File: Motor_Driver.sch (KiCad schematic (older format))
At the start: 43 parts, among them CN3 CONN_HEADER_R_A_2POS_2.5MM, Q14 AOD4185, Q5 2N7002BK, Q6 2N7002BK, Q7 2N7002BK, U7 LMC6772AIMX-1, U8 VNH5019ATR-E, U9 LMC6772AIMX_2

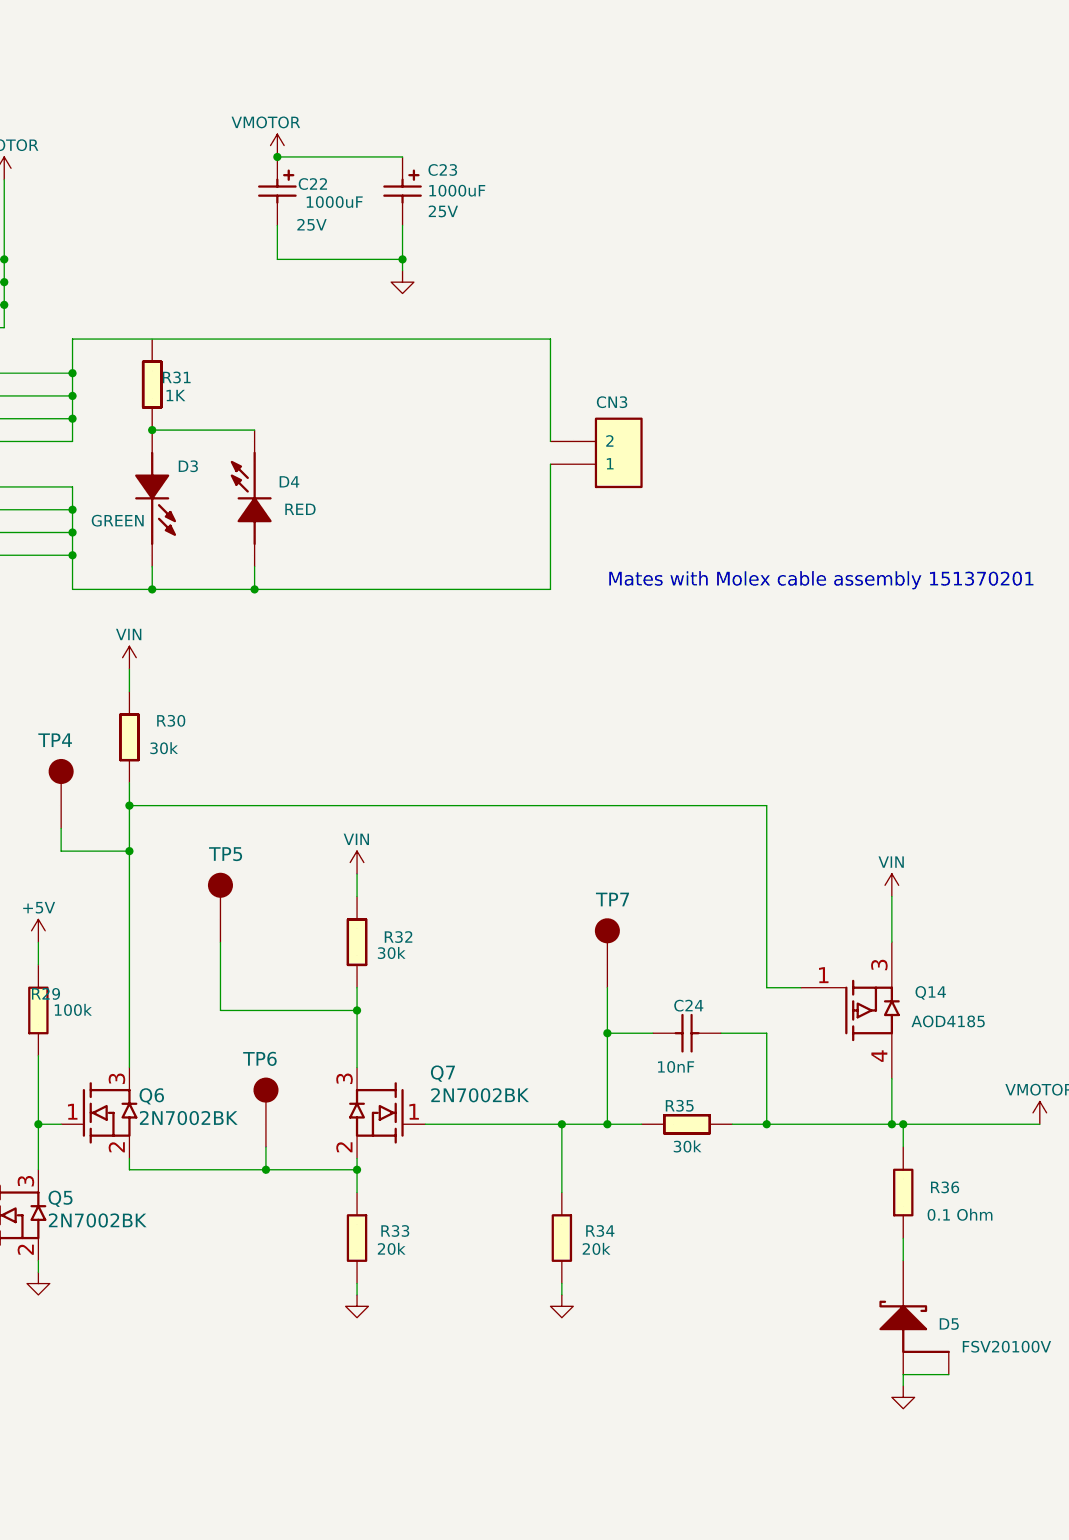
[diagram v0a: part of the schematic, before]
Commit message: Still had some text cleanups to do plus fixed a couple of minor circuit issues.
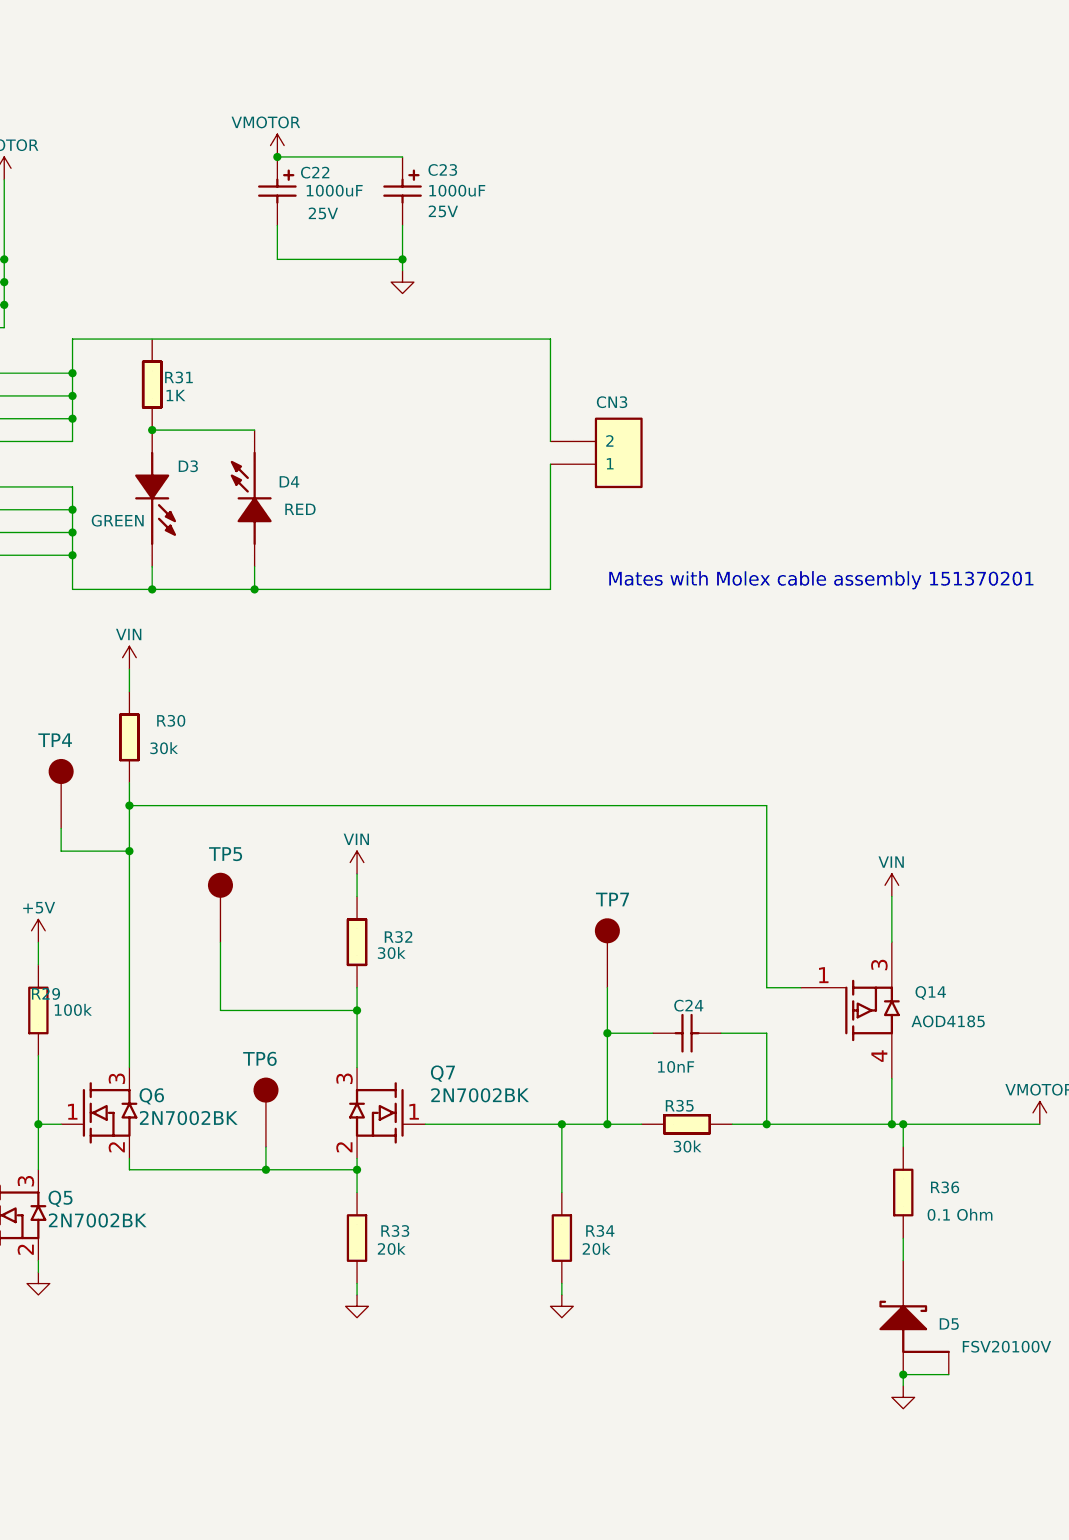
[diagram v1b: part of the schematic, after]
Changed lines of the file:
@@
 U 1 1 5F8DD0F1
 P 7050 1600
-F 0 "R31" V 7150 1540 50  0000 L BNN
+F 0 "R31" V 7150 1550 50  0000 L BNN
 F 1 "1K_0603_Chip_Resistor,_1%,_0.1W" V 7250 1550 50  0001 C CNN
 F 2 "" H 7350 1540 60  0001 C CNN
@@
 U 1 1 5F8DD0EF
 P 7500 700
-F 0 "C22" V 7650 790 50  0000 L BNN
+F 0 "C22" V 7600 800 50  0000 L BNN
 F 1 "1000uF_25V_Aluminium_SMD_Capacitor,_20%" V 7750 790 50  0001 C CNN
 F 2 "" H 7500 700 60  0001 C CNN
 F 3 "" H 7500 700 60  0001 C CNN
-F 4 "1000uF" V 7700 950 50  0000 C CNN "Val"
-F 5 "25V" V 7800 850 50  0000 C CNN "Voltage"
+F 4 "1000uF" V 7650 950 50  0000 C CNN "Val"
+F 5 "25V" V 7750 900 50  0000 C CNN "Voltage"
 	1    7500 700
 	0    1    1    0
@@
 Wire Wire Line
 	6950 1900 7400 1900
+Connection ~ 10250 6050
 $EndSCHEMATC

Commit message: Updating my local branch, wip Friday 10/30/20.  Got sucked into fixing up the libraries for the BOM...
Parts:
- removed U7: LMC6772AIMX-1, symbol OpenVent:LMC6772AIMX-1
- removed U9: LMC6772AIMX_2, symbol OpenVent:LMC6772AIMX_2
- added U7: LMC6772AIMX, Package_SO:SO-8_3.9x4.9mm_P1.27mm, symbol OpenVent:LMC6772AIMX
- C21: footprint (none) -> Capacitor_SMD:C_0603_1608Metric
- C24: footprint (none) -> Capacitor_SMD:C_0603_1608Metric; Voltage Rating 50V -> (none)
- CN3: Manufacturer Molex -> (none); ManufacturerPN 0534260210 -> (none); Mfr (none) -> Molex; Mfr_PN (none) -> 0534260210
- D3: footprint (none) -> LED_SMD:LED_0603_1608Metric; Spice Prefix D -> (none)
- D4: footprint (none) -> LED_SMD:LED_0603_1608Metric
- D5: footprint (none) -> Package_TO_SOT_SMD:TO-277A; Current (none) -> 20A; Desc (none) -> DIODE SCHOTTKY 100V 20A TO277-3; Detailed (none) -> Diode Schottky 20A Surface Mount TO-277-3; DistName (none) -> DigiKey; Dist_PN (none) -> FSV20100VTR-ND; Mfr (none) -> ON Semiconductor; Mfr_PN (none) -> FSV20100V; Voltage (none) -> 100V
- Q14: footprint (none) -> Package_TO_SOT_SMD:TO-252-2; Current (none) -> 40A; Desc (none) -> MOSFET P-CH 40V 40A TO252; DistName (none) -> DigiKey; Dist_PN (none) -> 785-1222-2-ND; Mfr (none) -> Alpha & Omega Semiconductor Inc.; Voltage (none) -> 40V
- Q5, Q6, Q7: footprint (none) -> Package_TO_SOT_SMD:SOT-23
- R16, R17, R18, R19, R20, R21, R22, R23, R24, R25, R27, R28, R29, R30, R31, R32, R33, R34, R35, R36: footprint (none) -> Resistor_SMD:R_0603_1608Metric
- R26: Manufacturer Vishay Dale -> (none); Mfr (none) -> Vishay Dale
- TP1, TP2, TP3, TP4, TP5, TP6, TP7: value ~ -> Test_Point_PTH; footprint (none) -> TestPoint:TestPoint_Pad_2.0x2.0mm
- U8: footprint (none) -> Package_SO:ST_MultiPowerSO-30; Desc (none) -> IC MTR DRV 5.5-24V MULTIPWRSO-30; Detailed (none) -> - Motor Driver Power MOSFET Parallel, PWM MultiPowerSO-30; DistName (none) -> DigiKey; Dist_PN (none) -> 497-13073-2-ND; Manufacturer ST Microelectronics -> (none); ManufacturerPN VNH5019ATR-E -> (none); Mfr (none) -> STMicroelectronics; Mfr_PN (none) -> VNH5019ATR-E

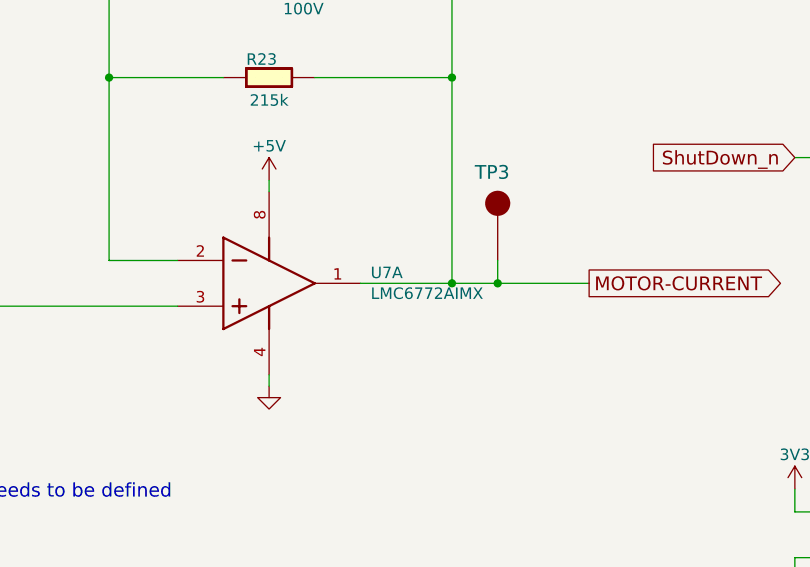
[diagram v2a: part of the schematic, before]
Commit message: Continuing on with library updates.  Started to fix up the USB interfaces.
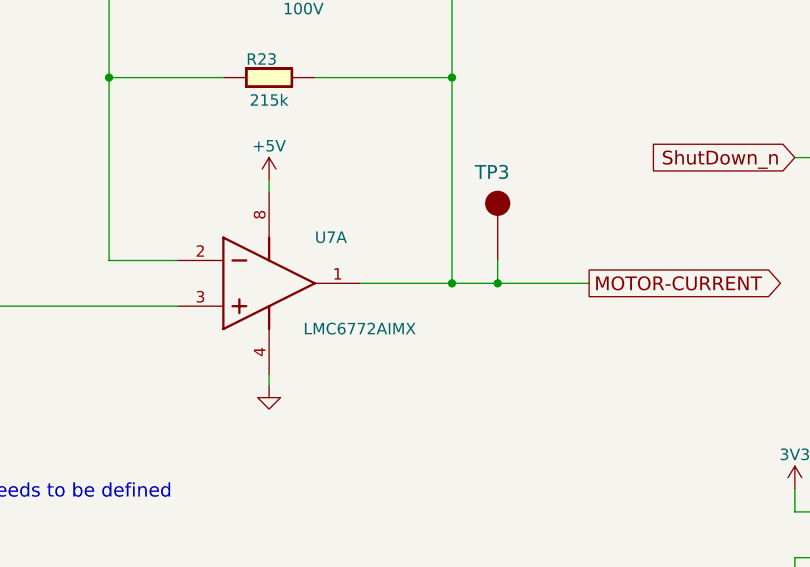
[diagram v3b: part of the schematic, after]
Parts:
- C22, C23: footprint (none) -> Capacitor_SMD:CP_Elec_10x10; Desc (none) -> CAP ALUM 1000UF 20% 25V SMD; Detailed (none) -> Aluminum Electrolytic Capacitors Radial, Can - SMD 60mOhm @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; DistName (none) -> DigiKey; Dist_PN (none) -> 565-5120-2-ND; Mfr (none) -> United Chemi-Con; Mfr_PN (none) -> EMZS250ARA102MJA0G; Tolerance (none) -> 20%
- D3: Desc (none) -> LED YELLOW/GREEN 1608 SMD; Detailed (none) -> Yellow-Green 572nm LED Indication - Discrete 2.2V 0603 (160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; DistName (none) -> DigiKey; Dist_PN (none) -> SML-D12M8WT86CTR-ND; Mfr (none) -> Rohm Semiconductor
- D4: Desc (none) -> LED RED CLEAR CHIP SMD; Detailed (none) -> Red 631nm LED Indication - Discrete 2V 0603 (1608 Metric); DistName (none) -> DigiKey; Dist_PN (none) -> 160-1830-2-ND; Mfr (none) -> Lite-On Inc.
- Q5, Q6, Q7: Current (none) -> 350mA; Desc (none) -> MOSFET N-CH 60V 350MA SOT23; Detailed (none) -> N-Channel 350mA (Ta) 370mW (Ta) Surface Mount TO-236AB; DistName (none) -> DigiKey; Dist_PN (none) -> 1727-4789-2-ND; Mfr (none) -> Nexperia USA Inc.; Mfr_PN (none) -> 2N7002BK,215; Voltage (none) -> 60V
- R20: value 1k -> 1K_0603_Chip_Resistor,_1%,_0.1W; Watt (none) -> 0.1W
- R26: Tolerance (none) -> 1%; Val (none) -> 0.025Ohm; Watt (none) -> 1.0W
- U8: Detailed - Motor Driver Power MOSFET Parallel, PWM MultiPowerSO-30 -> Motor Driver Power MOSFET Parallel, PWM MultiPowerSO-30
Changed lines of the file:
@@
 P 2800 1350
 F 0 "R20" H 2800 1300 50  0000 L BNN
-F 1 "1k" H 3000 1100 50  0001 L BNN
+F 1 "1K_0603_Chip_Resistor,_1%,_0.1W" H 3000 1100 50  0001 C CNN
 F 2 "Resistor_SMD:R_0603_1608Metric" H 2750 1100 60  0001 C CNN
-F 3 "" H 2750 1100 50  0001 C CNN
+F 3 "" H 2750 1100 60  0001 C CNN
 F 4 "1%" V 1150 -1350 50  0001 C CNN "Tolerance"
 F 5 "1K" H 2950 1150 50  0000 C CNN "Val"
+F 6 "0.1W" H 2800 1350 50  0001 C CNN "Watt"
 	1    2800 1350
 	1    0    0    -1
@@
 F 2 "" H 8700 1950 50  0001 C CNN
 F 3 "" H 8700 1950 50  0001 C CNN
-F 4 "" V 850 -1550 60  0001 C CNN "ManufacturerPN"
-F 5 "" V 850 -1550 60  0001 C CNN "Manufacturer"
-F 6 "Molex" H 8700 1950 50  0001 C CNN "Mfr"
-F 7 "0534260210" H 8700 1950 50  0001 C CNN "Mfr_PN"
+F 4 "Molex" H 8700 1950 50  0001 C CNN "Mfr"
+F 5 "0534260210" H 8700 1950 50  0001 C CNN "Mfr_PN"
 	1    8700 1950
 	1    0    0    1
@@
 F 2 "Package_SO:ST_MultiPowerSO-30" H 4850 1050 50  0001 C CNN
 F 3 "http://www.st.com/content/ccc/resource/technical/document/datasheet/1c/26/60/a8/3e/70/4c/e1/CD00234623.pdf/files/CD00234623.pdf/jcr:content/translations/en.CD00234623.pdf" H 4850 1050 60  0001 C CNN
-F 4 "" V 1150 -1350 60  0001 C CNN "Manufacturer"
-F 5 "" V 1150 -1350 60  0001 C CNN "ManufacturerPN"
-F 6 "STMicroelectronics" H 4850 1050 50  0001 C CNN "Mfr"
-F 7 "VNH5019ATR-E" H 4850 1050 50  0001 C CNN "Mfr_PN"
-F 8 "IC MTR DRV 5.5-24V MULTIPWRSO-30" H 4850 1050 50  0001 C CNN "Desc"
-F 9 "- Motor Driver Power MOSFET Parallel, PWM MultiPowerSO-30" H 4850 1050 50  0001 C CNN "Detailed"
-F 10 "DigiKey" H 4850 1050 50  0001 C CNN "DistName"
-F 11 "497-13073-2-ND" H 4850 1050 50  0001 C CNN "Dist_PN"
+F 4 "STMicroelectronics" H 4850 1050 50  0001 C CNN "Mfr"
+F 5 "VNH5019ATR-E" H 4850 1050 50  0001 C CNN "Mfr_PN"
+F 6 "IC MTR DRV 5.5-24V MULTIPWRSO-30" H 4850 1050 50  0001 C CNN "Desc"
+F 7 "Motor Driver Power MOSFET Parallel, PWM MultiPowerSO-30" H 4850 1050 50  0001 C CNN "Detailed"
+F 8 "DigiKey" H 4850 1050 50  0001 C CNN "DistName"
+F 9 "497-13073-2-ND" H 4850 1050 50  0001 C CNN "Dist_PN"
 	1    4850 1050
 	1    0    0    -1
@@
 F 2 "Resistor_SMD:R_2010_5025Metric" H 4422 3300 60  0001 C CNN
 F 3 "" H 4422 3300 60  0001 C CNN
-F 4 "" H 4250 3550 50  0001 C CNN "Manufacturer"
-F 5 "WSL2010R0250FEA18" H 4250 3550 50  0001 C CNN "Mfr_PN"
-F 6 "Vishay Dale" H 4250 3550 50  0001 C CNN "Mfr"
+F 4 "WSL2010R0250FEA18" H 4250 3550 50  0001 C CNN "Mfr_PN"
+F 5 "Vishay Dale" H 4250 3550 50  0001 C CNN "Mfr"
+F 6 "1%" H 4250 3550 50  0001 C CNN "Tolerance"
+F 7 "0.025Ohm" H 4250 3550 50  0001 C CNN "Val"
+F 8 "1.0W" H 4250 3550 50  0001 C CNN "Watt"
 	1    4250 3550
 	0    -1   -1   0
@@
 F 1 "LED_Red_0603_SMD" V 7710 2420 50  0001 C CNN
 F 2 "LED_SMD:LED_0603_1608Metric" H 7710 2420 50  0001 C CNN
-F 3 "" H 7710 2420 50  0001 C CNN
+F 3 "http://optoelectronics.liteon.com/upload/download/DS22-2005-077/LTST-C193KRKT-5A.PDF" H 7710 2420 50  0001 C CNN
 F 4 "LTST-C193KRKT-5A" V 1150 -1350 50  0001 C CNN "Mfr_PN"
 F 5 "RED" V 7650 2300 50  0000 C CNN "Colour"
+F 6 "LED RED CLEAR CHIP SMD" H 7400 2500 50  0001 C CNN "Desc"
+F 7 "Red 631nm LED Indication - Discrete 2V 0603 (1608 Metric)" H 7400 2500 50  0001 C CNN "Detailed"
+F 8 "DigiKey" H 7400 2500 50  0001 C CNN "DistName"
+F 9 "160-1830-2-ND" H 7400 2500 50  0001 C CNN "Dist_PN"
+F 10 "Lite-On Inc." H 7400 2500 50  0001 C CNN "Mfr"
 	1    7400 2500
 	0    -1   -1   0
@@
 F 1 "LED_GREEN_0603_SMD" V 7240 2010 60  0001 C CNN
 F 2 "LED_SMD:LED_0603_1608Metric" H 7240 2010 50  0001 C CNN
-F 3 "" H 7240 2010 50  0001 C CNN
+F 3 "https://www.rohm.com/datasheet/SML-D12M8W(C)/sml-d12x8(c)-e" H 7240 2010 50  0001 C CNN
 F 4 "SML-D12M8WT86C" V 1150 -1350 60  0001 C CNN "Mfr_PN"
-F 5 "" V 1150 -1350 60  0001 C CNN "Spice Prefix"
-F 6 "GREEN" V 7350 1750 50  0000 C CNN "Colour"
+F 5 "GREEN" V 7350 1750 50  0000 C CNN "Colour"
+F 6 "LED YELLOW/GREEN 1608 SMD" H 6950 1900 50  0001 C CNN "Desc"
+F 7 "Yellow-Green 572nm LED Indication - Discrete 2.2V 0603 (1608 Metric)" H 6950 1900 50  0001 C CNN "Detailed"
+F 8 "DigiKey" H 6950 1900 50  0001 C CNN "DistName"
+F 9 "SML-D12M8WT86CTR-ND" H 6950 1900 50  0001 C CNN "Dist_PN"
+F 10 "Rohm Semiconductor" H 6950 1900 50  0001 C CNN "Mfr"
 	1    6950 1900
 	0    1    1    0
@@
 F 0 "C22" V 7600 800 50  0000 L BNN
 F 1 "1000uF_25V_Aluminium_SMD_Capacitor,_20%" V 7750 790 50  0001 C CNN
-F 2 "" H 7500 700 60  0001 C CNN
-F 3 "" H 7500 700 60  0001 C CNN
+F 2 "Capacitor_SMD:CP_Elec_10x10" H 7500 700 60  0001 C CNN
+F 3 "https://www.digikey.com/en/product-highlight/u/united-chemi-con/mzs-series-aluminum-electrolytic-capacitors" H 7500 700 60  0001 C CNN
 F 4 "1000uF" V 7650 950 50  0000 C CNN "Val"
 F 5 "25V" V 7750 900 50  0000 C CNN "Voltage"
+F 6 "CAP ALUM 1000UF 20% 25V SMD" H 7500 700 50  0001 C CNN "Desc"
+F 7 "Aluminum Electrolytic Capacitors Radial, Can - SMD 60mOhm @ 100kHz 2000 Hrs @ 105°C" H 7500 700 50  0001 C CNN "Detailed"
+F 8 "DigiKey" H 7500 700 50  0001 C CNN "DistName"
+F 9 "565-5120-2-ND" H 7500 700 50  0001 C CNN "Dist_PN"
+F 10 "United Chemi-Con" H 7500 700 50  0001 C CNN "Mfr"
+F 11 "EMZS250ARA102MJA0G" H 7500 700 50  0001 C CNN "Mfr_PN"
+F 12 "20%" H 7500 700 50  0001 C CNN "Tolerance"
 	1    7500 700
 	0    1    1    0
@@
 F 1 "2N7002BK" H 8170 4540 50  0000 L BNN
 F 2 "Package_TO_SOT_SMD:SOT-23" H 8170 4540 50  0001 C CNN
-F 3 "" H 8170 4540 50  0001 C CNN
+F 3 "https://assets.nexperia.com/documents/data-sheet/2N7002BK.pdf" H 8170 4540 50  0001 C CNN
+F 4 "350mA" H 7850 4700 50  0001 C CNN "Current"
+F 5 "MOSFET N-CH 60V 350MA SOT23" H 7850 4700 50  0001 C CNN "Desc"
+F 6 "N-Channel 350mA (Ta) 370mW (Ta) Surface Mount TO-236AB" H 7850 4700 50  0001 C CNN "Detailed"
+F 7 "DigiKey" H 7850 4700 50  0001 C CNN "DistName"
+F 8 "1727-4789-2-ND" H 7850 4700 50  0001 C CNN "Dist_PN"
+F 9 "Nexperia USA Inc." H 7850 4700 50  0001 C CNN "Mfr"
+F 10 "2N7002BK,215" H 7850 4700 50  0001 C CNN "Mfr_PN"
+F 11 "60V" H 7850 4700 50  0001 C CNN "Voltage"
 	1    7850 4700
 	1    0    0    -1
@@
 F 2 "Capacitor_SMD:C_0603_1608Metric" H 9240 4160 50  0001 C CNN
 F 3 "" H 9240 4160 50  0001 C CNN
-F 4 "" V 1650 -1850 60  0001 C CNN "Voltage Rating"
-F 5 "10%" H 9250 4450 50  0001 C CNN "Tolerance"
-F 6 "10nF" H 9250 4200 50  0000 C CNN "Val"
-F 7 "50V" H 9250 4450 50  0001 C CNN "Voltage"
+F 4 "10%" H 9250 4450 50  0001 C CNN "Tolerance"
+F 5 "10nF" H 9250 4200 50  0000 C CNN "Val"
+F 6 "50V" H 9250 4450 50  0001 C CNN "Voltage"
 	1    9250 4450
 	1    0    0    -1
@@
 F 1 "2N7002BK" H 6810 4440 50  0000 R BNN
 F 2 "Package_TO_SOT_SMD:SOT-23" H 6810 4440 50  0001 C CNN
-F 3 "" H 6810 4440 50  0001 C CNN
+F 3 "https://assets.nexperia.com/documents/data-sheet/2N7002BK.pdf" H 6810 4440 50  0001 C CNN
+F 4 "350mA" H 6850 4700 50  0001 C CNN "Current"
+F 5 "MOSFET N-CH 60V 350MA SOT23" H 6850 4700 50  0001 C CNN "Desc"
+F 6 "N-Channel 350mA (Ta) 370mW (Ta) Surface Mount TO-236AB" H 6850 4700 50  0001 C CNN "Detailed"
+F 7 "DigiKey" H 6850 4700 50  0001 C CNN "DistName"
+F 8 "1727-4789-2-ND" H 6850 4700 50  0001 C CNN "Dist_PN"
+F 9 "Nexperia USA Inc." H 6850 4700 50  0001 C CNN "Mfr"
+F 10 "2N7002BK,215" H 6850 4700 50  0001 C CNN "Mfr_PN"
+F 11 "60V" H 6850 4700 50  0001 C CNN "Voltage"
 	1    6850 4700
 	-1   0    0    -1
@@
 F 1 "2N7002BK" H 6410 4890 50  0000 R BNN
 F 2 "Package_TO_SOT_SMD:SOT-23" H 6410 4890 50  0001 C CNN
-F 3 "" H 6410 4890 50  0001 C CNN
+F 3 "https://assets.nexperia.com/documents/data-sheet/2N7002BK.pdf" H 6410 4890 50  0001 C CNN
+F 4 "350mA" H 6450 5150 50  0001 C CNN "Current"
+F 5 "MOSFET N-CH 60V 350MA SOT23" H 6450 5150 50  0001 C CNN "Desc"
+F 6 "N-Channel 350mA (Ta) 370mW (Ta) Surface Mount TO-236AB" H 6450 5150 50  0001 C CNN "Detailed"
+F 7 "DigiKey" H 6450 5150 50  0001 C CNN "DistName"
+F 8 "1727-4789-2-ND" H 6450 5150 50  0001 C CNN "Dist_PN"
+F 9 "Nexperia USA Inc." H 6450 5150 50  0001 C CNN "Mfr"
+F 10 "2N7002BK,215" H 6450 5150 50  0001 C CNN "Mfr_PN"
+F 11 "60V" H 6450 5150 50  0001 C CNN "Voltage"
 	1    6450 5150
 	-1   0    0    -1
@@
 F 0 "C23" V 8109 810 50  0000 L CNN
 F 1 "1000uF_25V_Aluminium_SMD_Capacitor,_20%" H 8050 700 50  0001 C CNN
-F 2 "" H 8050 700 60  0001 C CNN
-F 3 "" H 8050 700 60  0001 C CNN
+F 2 "Capacitor_SMD:CP_Elec_10x10" H 8050 700 60  0001 C CNN
+F 3 "https://www.digikey.com/en/product-highlight/u/united-chemi-con/mzs-series-aluminum-electrolytic-capacitors" H 8050 700 60  0001 C CNN
 F 4 "1000uF" V 8200 810 50  0000 L CNN "Val"
 F 5 "25V" V 8291 810 50  0000 L CNN "Voltage"
+F 6 "CAP ALUM 1000UF 20% 25V SMD" H 8050 700 50  0001 C CNN "Desc"
+F 7 "Aluminum Electrolytic Capacitors Radial, Can - SMD 60mOhm @ 100kHz 2000 Hrs @ 105°C" H 8050 700 50  0001 C CNN "Detailed"
+F 8 "DigiKey" H 8050 700 50  0001 C CNN "DistName"
+F 9 "565-5120-2-ND" H 8050 700 50  0001 C CNN "Dist_PN"
+F 10 "United Chemi-Con" H 8050 700 50  0001 C CNN "Mfr"
+F 11 "EMZS250ARA102MJA0G" H 8050 700 50  0001 C CNN "Mfr_PN"
+F 12 "20%" H 8050 700 50  0001 C CNN "Tolerance"
 	1    8050 700
 	0    1    1    0
@@
 U 1 1 5FAA14CD
 P 2450 6050
-F 0 "U7" H 3294 6196 50  0000 L CNN
-F 1 "LMC6772AIMX" H 3294 6105 50  0000 L CNN
+F 0 "U7" H 3050 6350 50  0000 L CNN
+F 1 "LMC6772AIMX" H 3000 5950 50  0000 L CNN
 F 2 "Package_SO:SO-8_3.9x4.9mm_P1.27mm" H 2450 6050 50  0001 C CNN
 F 3 "http://www.ti.com/general/docs/suppproductinfo.tsp?distId=10&gotoUrl=http%3A%2F%2Fwww.ti.com%2Flit%2Fgpn%2Flmc6772" H 2450 6050 50  0001 C CNN
